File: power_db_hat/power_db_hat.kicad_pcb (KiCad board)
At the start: 4 copper layers, 65 x 56 mm, 151 parts, among them J1 Conn_01x02_Pin, J10 Screw_Terminal_01x02, J11 Conn_01x03_Pin, J12 Conn_01x03_Pin, J15 Screw_Terminal_01x02, J16 Screw_Terminal_01x02, J2 BAT2, J3 Screw_Terminal_01x02, J4 Screw_Terminal_01x02, J5 24V_out, J6 Conn_01x02_Pin, J7 Screw_Terminal_01x02, J8 BAT1, Q1 FDS6681Z, Q2 FDS6681Z, Q6 SIS468DN, Q7 SIS468DN, U1 INA3221, U2 LDD-700LS, U3 MAX17506ATP+T, U4 TL431DBZ, U5 MAX17506ATP+T, U6 LDD-700LS, U7 B2B pins, U8 DRV8212P, U9 DRV8212P

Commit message: lol
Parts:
- removed D52: D_Schottky, Diode_SMD:D_SMA-SMB_Universal_Handsoldering
- removed D6: D_Schottky, Diode_SMD:D_SMB_Handsoldering
- added J3: Screw_Terminal_01x02, TerminalBlock:TerminalBlock_Xinya_XY308-2.54-2P_1x02_P2.54mm_Horizontal, F.Cu at (2.04, 3.62)
- added J7: Screw_Terminal_01x02, TerminalBlock:TerminalBlock_Xinya_XY308-2.54-2P_1x02_P2.54mm_Horizontal, F.Cu at (9.69, 3.62)
- added Q3: BC847, Package_TO_SOT_SMD:SOT-23, F.Cu at (105.9, 146.1)
- added Q4: FDS6681Z, FDS6681Z:FDS6681Z_SOP-8, F.Cu at (107.8, 139.9)
- added R3: 10k, Resistor_SMD:R_0603_1608Metric_Pad0.98x0.95mm_HandSolder, F.Cu at (124.7, 142.8)
- added R4: 100k, Resistor_SMD:R_0603_1608Metric_Pad0.98x0.95mm_HandSolder, F.Cu at (124.7, 145.3)
- added R5: 100k, Resistor_SMD:R_0603_1608Metric_Pad0.98x0.95mm_HandSolder, F.Cu at (124.7, 147.8)
- C10, C19, C20, C25, C26, C5, JP10, JP11, JP12, JP2, JP3, JP9, R1, U1: moved to B.Cu
- C17, C27, C28: moved to F.Cu
- L1: footprint IND_B82477G4472M000:IND_B82477G4472M000 -> B82477G4472M000:IND_B82477G4472M000
- L2: footprint IND_B82477G4472M000:IND_B82477G4472M000 -> Inductor_SMD:L_TDK_VLS6045EX_VLS6045AF; moved to B.Cu
- Q6, Q7: footprint Package_SO:Vishay_PowerPAK_1212-8_Single -> SiS468DN:Vishay_PowerPAK_1212-8_Single
- U8, U9: footprint Package_SON:WSON-8-1EP_2x2mm_P0.5mm_EP0.9x1.6mm_ThermalVias -> Package_SON:WSON-8-1EP_2x2mm_P0.5mm_EP0.9x1.6mm; moved to B.Cu
- moved C16 114.4 mm to (123.1, 73.0)
- moved C29 108.7 mm to (126.9, 65.0), turned to 0 degrees
- moved R20 108.2 mm to (119.5, 73.0), turned to 0 degrees
- moved R19 100.9 mm to (126.0, 62.0), turned to 90 degrees
- moved C39 97.9 mm to (133.4, 59.5)
- moved C41 96.8 mm to (133.4, 62.0)
- moved C43 94.0 mm to (133.4, 64.5)
- moved L2 82.4 mm to (139.5, 64.0), turned to 90 degrees
- moved JP10 80.3 mm to (129.5, 73.5), turned to 180 degrees
- moved C17 77.3 mm to (119.5, 58.5), turned to 90 degrees
- moved C27 76.4 mm to (122.0, 58.5), turned to 90 degrees
- moved C28 75.6 mm to (124.5, 58.5), turned to 90 degrees
- moved R44 75.3 mm to (147.4, 70.0)
- moved R66 75.1 mm to (147.4, 72.5)
- moved Q6 71.6 mm to (147.0, 66.0)
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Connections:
- U8 pad 2: Net-(J3-Pin_1) -> Net-(J3-Pin_2)
- U8 pad 3: Net-(J3-Pin_2) -> Net-(J3-Pin_1)
- U9 pad 2: Net-(J7-Pin_1) -> Net-(J7-Pin_2)
- U9 pad 3: Net-(J7-Pin_2) -> Net-(J7-Pin_1)
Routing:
- net Net-(U3-EN/UVLO): track 0.00 -> 7.21 mm
- net Net-(Q7-D): track 0.00 -> 7.05 mm, vias 0 -> 4
- net +24V: track 3.16 -> 10.2 mm
- net Net-(U3-EXTVCC): track 0.00 -> 5.52 mm
- net Net-(U3-SS): track 0.00 -> 2.97 mm
- net Net-(U3-*RESET): track 0.00 -> 2.67 mm
- net Net-(JP10-A): track 0.00 -> 2.61 mm
- net Net-(U3-BST): track 0.00 -> 2.48 mm
- net Net-(Q7-G): track 0.00 -> 2.38 mm
- net Net-(U3-DL): track 0.00 -> 2.07 mm
- added copper zone on F.Cu, net +24V
- added copper zone on B.Cu, net Net-(Q7-D)
- added copper zone on F.Cu, net Net-(Q7-D)

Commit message: lol
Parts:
- removed JP4, JP6: SolderJumper_2_Open, Jumper:SolderJumper-2_P1.3mm_Open_TrianglePad1.0x1.5mm
- moved R29 105.8 mm to (97.1, 39.5)
- moved R5 95.6 mm to (117.0, 52.5), turned to 180 degrees
- moved Q3 95.4 mm to (122.0, 52.0), turned to 180 degrees
- moved R4 91.3 mm to (127.5, 54.0), turned to 90 degrees
- moved R3 88.8 mm to (125.5, 54.0), turned to -90 degrees
- moved Q4 84.1 mm to (118.5, 56.5), turned to 180 degrees
- moved R34 71.5 mm to (120.5, 54.5), turned to 90 degrees
- moved JP9 53.2 mm to (202.4, 88.7)
- moved L2 53.2 mm to (190.1, 80.2)
- moved Q6 53.2 mm to (197.6, 82.2)
- moved R44 53.2 mm to (198.0, 86.2)
- moved R66 53.2 mm to (198.0, 88.7)
- moved U1 53.2 mm to (194.8, 94.5)
- moved U5 53.2 mm to (190.1, 87.7)
- moved U8 53.2 mm to (204.6, 95.5)
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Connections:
- R33 pad 1: /power/VOUT_12V -> +12V
- R34 pad 1: /power/5V_OUT -> +5V
- U1 pad 1: /power/5V_OUT -> +5V
- U1 pad 14: /power/VOUT_12V -> +12V
- U7 pad 10b: GND -> +5V
- U7 pad 11b: +3V3 -> /I2C_SDA
- U7 pad 12b: /I2C_SCL -> +5V
- U7 pad 1b: +5V -> GND
- U7 pad 2b: +5V -> GND
- U7 pad 6b: GND -> +5V
- U7 pad 6c: GND -> unconnected-(U7-Pad6c)
- U7 pad 7b: +5V -> /I2C_SCL
- U7 pad 8b: /I2C_SDA -> +5V
- U7 pad 8c: GND -> +3V3
- U7 pad 9b: +3V3 -> GND
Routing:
- net +24V: track 10.2 -> 1.29 mm, vias 22 -> 24
- net Net-(Q7-D): track 7.05 -> 3.33 mm, vias 4 -> 0
- net Net-(JP10-A): track 2.61 -> 0.00 mm
- net Net-(Q7-G): track 2.38 -> 0.00 mm
- net Net-(U3-EN/UVLO): track 7.21 -> 5.21 mm
- removed copper zone on B.Cu, net Net-(Q7-D)
- removed copper zone on F.Cu, net Net-(Q7-D)

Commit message: LMAO
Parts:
- removed the J3 at (2.04, 3.62)
- removed the J7 at (9.69, 3.62)
- C10, C19, C20, C25, C26, C5, JP11, JP12, JP2, JP3, JP9, L2, R1, R34, U1, U8, U9: moved to F.Cu
- moved U1 104.9 mm to (90.0, 90.5), turned to 0 degrees
- moved C39 89.9 mm to (231.1, 63.7)
- moved C41 89.4 mm to (228.6, 79.0)
- moved C43 85.6 mm to (226.8, 53.7)
- moved C10 69.0 mm to (238.2, 121.8), turned to 0 degrees
- moved C19 69.0 mm to (238.2, 124.3), turned to 0 degrees
- moved C5 69.0 mm to (238.2, 119.3), turned to 0 degrees
- moved R1 69.0 mm to (238.2, 139.3), turned to 0 degrees
- moved R2 69.0 mm to (238.2, 141.8)
- moved JP9 47.1 mm to (181.7, 131.0)
- moved JP11 44.1 mm to (181.7, 119.9), turned to 0 degrees
- moved JP12 44.1 mm to (181.7, 123.4), turned to 0 degrees
- moved Q6 35.8 mm to (217.3, 52.4)
- moved R44 33.1 mm to (222.4, 63.7)
- moved L2 32.7 mm to (210.5, 105.8), turned to 0 degrees
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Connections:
- C16 pad 2: Net-(Q7-D) -> /power/5V_SNS+
- C37 pad 2: Net-(Q6-D) -> /power/12V_SNS+
- C39 pad 1: /power/12V_SNS -> +12V
- C41 pad 1: /power/12V_SNS -> +12V
- C43 pad 1: /power/12V_SNS -> +12V
- L1 pad 1: Net-(Q7-D) -> /power/5V_SNS-
- L2 pad 1: Net-(Q6-D) -> /power/12V_SNS-
- L2 pad 2: /power/12V_SNS -> +12V
- Q4 pad 3: /power/5V_SNS -> +5V
- Q6 pad 1: Net-(Q6-D) -> /power/12V_SNS+
- Q7 pad 1: Net-(Q7-D) -> /power/5V_SNS+
- R33 pad 1: +12V -> /power/12V_SNS-
- R33 pad 2: /power/12V_SNS -> /power/12V_SNS+
- R34 pad 1: +5V -> /power/5V_SNS-
- R34 pad 2: /power/5V_SNS -> /power/5V_SNS+
- R35 pad 1: /power/12V_SNS -> +12V
- R38 pad 1: /power/12V_SNS -> +12V
- R42 pad 2: /power/12V_SNS -> +12V
- R5 pad 2: /power/5V_SNS -> +5V
- U1 pad 1: +5V -> /power/5V_SNS-
- U1 pad 14: +12V -> /power/12V_SNS+
- U1 pad 15: /power/12V_SNS -> /power/12V_SNS-
- U1 pad 2: /power/5V_SNS -> /power/5V_SNS+
- U3 pad 17: Net-(Q7-D) -> /power/5V_SNS+
- U3 pad 18: Net-(Q7-D) -> /power/5V_SNS+
- U3 pad 19: Net-(Q7-D) -> /power/5V_SNS+
- U5 pad 17: Net-(Q6-D) -> /power/12V_SNS+
- U5 pad 18: Net-(Q6-D) -> /power/12V_SNS+
- U5 pad 19: Net-(Q6-D) -> /power/12V_SNS+
- U7 pad 10b: +5V -> GND
- U7 pad 12b: +5V -> /I2C_SCL
- U7 pad 1b: GND -> +5V
- U7 pad 2b: GND -> +5V
- U7 pad 7b: /I2C_SCL -> +5V
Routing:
- net +24V: track 1.29 -> 7.05 mm, vias 24 -> 0
- net Net-(Q7-D): track 3.33 -> 0.00 mm
- net /power/5V_SNS+: track 0.00 -> 3.33 mm
- net Net-(JP10-A): track 0.00 -> 2.61 mm
- net Net-(U3-EN/UVLO): track 5.21 -> 7.21 mm
- net Net-(U3-VCC): track 2.53 -> 2.02 mm
- net +5V: vias 0 -> 5
- added copper zone on B.Cu, net +5V
- added copper zone on F.Cu, net +5V
- removed copper zone on F.Cu, net +24V

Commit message: lol
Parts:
- removed JP10, JP11, JP12, JP9: SolderJumper_2_Open, Jumper:SolderJumper-2_P1.3mm_Open_TrianglePad1.0x1.5mm
- C10, C19, C20, C25, C26, C44, C5, JP2, JP3, R1, R2, U1, U8, U9: moved to B.Cu
- moved C44 126.6 mm to (133.4, 65.8), turned to 180 degrees
- moved C9 125.1 mm to (126.0, 68.8), turned to -90 degrees
- moved C11 122.4 mm to (128.5, 68.8), turned to -90 degrees
- moved C13 119.8 mm to (131.0, 68.8), turned to -90 degrees
- moved R1 106.3 mm to (152.2, 76.8), turned to 90 degrees
- moved R23 105.1 mm to (121.8, 61.2), turned to 90 degrees
- moved R22 102.8 mm to (124.0, 61.2), turned to -90 degrees
- moved R2 102.1 mm to (152.6, 86.2), turned to 180 degrees
- moved C10 96.5 mm to (154.0, 74.6), turned to 90 degrees
- moved C20 95.5 mm to (152.6, 84.4), turned to 180 degrees
- moved C19 94.8 mm to (156.8, 75.6), turned to 180 degrees
- moved C26 94.5 mm to (156.6, 84.1), turned to 180 degrees
- moved C25 94.1 mm to (156.6, 82.4), turned to 180 degrees
- moved C5 93.2 mm to (156.8, 73.8), turned to 180 degrees
- moved U9 53.5 mm to (156.6, 86.2), turned to 180 degrees
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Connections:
- C16 pad 2: /power/5V_SNS+ -> Net-(Q7-D)
- C17 pad 1: /power/bucks/BUCK_OUT_5V -> /power/5V_SNS-
- C27 pad 1: /power/bucks/BUCK_OUT_5V -> /power/5V_SNS-
- C28 pad 1: /power/bucks/BUCK_OUT_5V -> /power/5V_SNS-
- L1 pad 1: /power/5V_SNS- -> Net-(Q7-D)
- L1 pad 2: /power/bucks/BUCK_OUT_5V -> /power/5V_SNS+
- Q4 pad 1: /power/bucks/BUCK_OUT_5V -> /power/5V_SNS-
- Q7 pad 1: /power/5V_SNS+ -> Net-(Q7-D)
- R19 pad 2: /power/bucks/BUCK_OUT -> /power/5V_SNS-
- R22 pad 1: /power/bucks/BUCK_OUT_5V -> /power/5V_SNS-
- R3 pad 2: /power/bucks/BUCK_OUT_5V -> /power/5V_SNS-
- R30 pad 1: /power/bucks/BUCK_OUT_5V -> /power/5V_SNS-
- R65 pad 1: Net-(JP10-A) -> +24V
- R66 pad 1: Net-(JP9-A) -> +24V
- U3 pad 17: /power/5V_SNS+ -> Net-(Q7-D)
- U3 pad 18: /power/5V_SNS+ -> Net-(Q7-D)
- U3 pad 19: /power/5V_SNS+ -> Net-(Q7-D)
- U7 pad 10c: GND -> /LED_PWM_1
- U7 pad 11c: /LED_PWM_2 -> GND
- U7 pad 12c: GND -> /LED_PWM_2
- U7 pad 1c: /MOTOR_1_A -> /SERVO_2
- U7 pad 2c: /SERVO_1 -> /MOTOR_1_B
- U7 pad 3c: /MOTOR_1_B -> /SERVO_1
- U7 pad 4c: /SERVO_2 -> /MOTOR_1_A
- U7 pad 5c: /MOTOR_2_A -> +3V3
- U7 pad 6c: unconnected-(U7-Pad6c) -> /MOTOR_2_B
- U7 pad 7c: /MOTOR_2_B -> +3V3
- U7 pad 8c: +3V3 -> /MOTOR_2_A
- U7 pad 9c: /LED_PWM_1 -> GND
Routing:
- net /MOTOR_2_A: track 0.00 -> 48.6 mm
- net +3V3: track 0.00 -> 47.9 mm, vias 0 -> 3
- net /MOTOR_2_B: track 0.00 -> 47.5 mm
- net /MOTOR_1_A: track 0.00 -> 42.2 mm
- net /MOTOR_1_B: track 0.00 -> 40.6 mm
- net /LED_PWM_2: track 0.00 -> 28.7 mm, vias 0 -> 1
- net /SERVO_1: track 0.00 -> 27.8 mm
- net /SERVO_2: track 0.00 -> 12.7 mm
- net /power/5V_SNS-: track 0.00 -> 7.71 mm
- net /expansion/V_ACT: track 0.00 -> 6.88 mm
- net GND: track 0.48 -> 5.37 mm
- net Net-(U3-FB): track 0.00 -> 4.80 mm
- net Net-(J3-Pin_1): track 0.00 -> 4.58 mm
- net Net-(J3-Pin_2): track 0.00 -> 3.98 mm
- net Net-(J7-Pin_2): track 0.00 -> 3.42 mm
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- added copper zone on F.Cu, net /power/5V_SNS+
- added copper zone on F.Cu, net /power/5V_SNS-
- added copper zone on B.Cu, net Net-(Q7-D)

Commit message: damo was here
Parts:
- removed C2, C4, C49: 100nF, Capacitor_SMD:C_0603_1608Metric_Pad1.08x0.95mm_HandSolder
- removed C50: 22uF, Capacitor_SMD:C_0603_1608Metric_Pad1.08x0.95mm_HandSolder
- removed D45, D46: TVS_3V3, Diode_SMD:D_0603_1608Metric_Pad1.05x0.95mm_HandSolder
- removed JP1: SolderJumper_2_Open, Jumper:SolderJumper-2_P1.3mm_Open_TrianglePad1.0x1.5mm
- removed R30, R38: 10k, Resistor_SMD:R_0603_1608Metric_Pad0.98x0.95mm_HandSolder
- C1, C23, C24, D41, L2: moved to B.Cu
- C44: moved to F.Cu
- moved R13 139.2 mm to (102.4, 57.9), turned to 180 degrees
- moved R12 139.1 mm to (102.4, 55.9), turned to 180 degrees
- moved R11 139.0 mm to (102.4, 53.9), turned to 180 degrees
- moved R10 137.3 mm to (102.4, 51.9), turned to 180 degrees
- moved C47 126.0 mm to (113.2, 45.1)
- moved C48 126.0 mm to (113.2, 47.6), turned to 180 degrees
- moved C23 125.5 mm to (134.3, 48.4), turned to -90 degrees
- moved C1 122.3 mm to (108.5, 74.7)
- moved C24 117.9 mm to (143.5, 48.8), turned to -90 degrees
- moved C30 116.8 mm to (132.3, 85.1)
- moved C43 113.2 mm to (116.8, 80.6), turned to 90 degrees
- moved C39 110.6 mm to (121.8, 80.6), turned to 90 degrees
- moved C41 109.3 mm to (119.3, 80.6), turned to 90 degrees
- moved C31 101.2 mm to (134.5, 71.0), turned to 90 degrees
- moved C32 100.6 mm to (132.5, 71.0), turned to 90 degrees
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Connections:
- C37 pad 2: /power/12V_SNS+ -> Net-(Q6-D)
- JP2 pad 1: /expansion/V_ACT -> +5V
- JP2 pad 2: +5V -> /expansion/V_ACT
- L2 pad 1: /power/12V_SNS- -> Net-(Q6-D)
- L2 pad 2: +12V -> /power/12V_SNS+
- Q6 pad 1: /power/12V_SNS+ -> Net-(Q6-D)
- R33 pad 1: /power/12V_SNS- -> +12V
- U1 pad 15: /power/12V_SNS- -> +12V
- U1 pad 4: Net-(JP1-B) -> +3V3
- U3 pad 6: Net-(U3-*RESET) -> unconnected-(U3-*RESET-Pad6)
- U5 pad 17: /power/12V_SNS+ -> Net-(Q6-D)
- U5 pad 18: /power/12V_SNS+ -> Net-(Q6-D)
- U5 pad 19: /power/12V_SNS+ -> Net-(Q6-D)
- U5 pad 6: Net-(U5-*RESET) -> unconnected-(U5-*RESET-Pad6)
- U7 pad 11b: /I2C_SDA -> /I2C_SCL
- U7 pad 11c: GND -> /IND
- U7 pad 12b: /I2C_SCL -> /I2C_SDA
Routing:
- net +12V: track 0.00 -> 145.9 mm, vias 0 -> 6
- net +3V3: track 47.9 -> 135.8 mm, vias 3 -> 7
- net /power/24V_SNS: track 2.48 -> 52.6 mm, vias 15 -> 12
- net +5V: track 0.00 -> 43.0 mm, vias 5 -> 35
- net /IND: track 0.00 -> 40.1 mm, vias 0 -> 1
- net /LED_PWM_1: track 3.30 -> 36.6 mm, vias 0 -> 1
- net /I2C_SDA: track 0.00 -> 30.3 mm
- net /power/12V_SNS+: track 0.00 -> 29.4 mm
- net /I2C_SCL: track 0.00 -> 28.3 mm
- net /power/5V_SNS-: track 7.71 -> 29.3 mm, vias 0 -> 1
- net +24V: track 4.31 -> 25.9 mm, vias 11 -> 21
- net /expansion/V_ACT: track 6.88 -> 23.2 mm, vias 0 -> 2
- net /power/5V_SNS+: track 0.00 -> 16.0 mm, vias 0 -> 1
- net Net-(Q6-G): track 0.00 -> 14.9 mm
- net Net-(JP5-A): track 0.00 -> 8.74 mm
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- added copper zone on F.Cu, net /VBAT1+
- added copper zone on In1.Cu, net /VBAT1+
- added copper zone on B.Cu, net GND
- added copper zone on F.Cu, net GND
- added copper zone on B.Cu, net Net-(Q6-D)
- added copper zone on F.Cu, net Net-(Q7-D)
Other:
- board text added: "{ "ViaStitching": "0.4", "stitch_zone_0": { "HSpacing": "3", "VSpacing": "3", "HOffset": "0", "VOffset": "0", "EdgeMargin": "0", "PadMargin": "0", "Clearance": "0", "ViaSize": "0.6", "ViaDrill": "0.3", "Randomize": false, "ClearOwn": true, "IncludeOtherLayers": true, "BlockFootprintZones": true, "AllowUnderPadSameNet": false, "TargetViaCountMode": false, "TargetViaCount": "100", "TargetPattern": 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"
- board text removed: "Extend PCB edge 0.5mm if using SMT header"

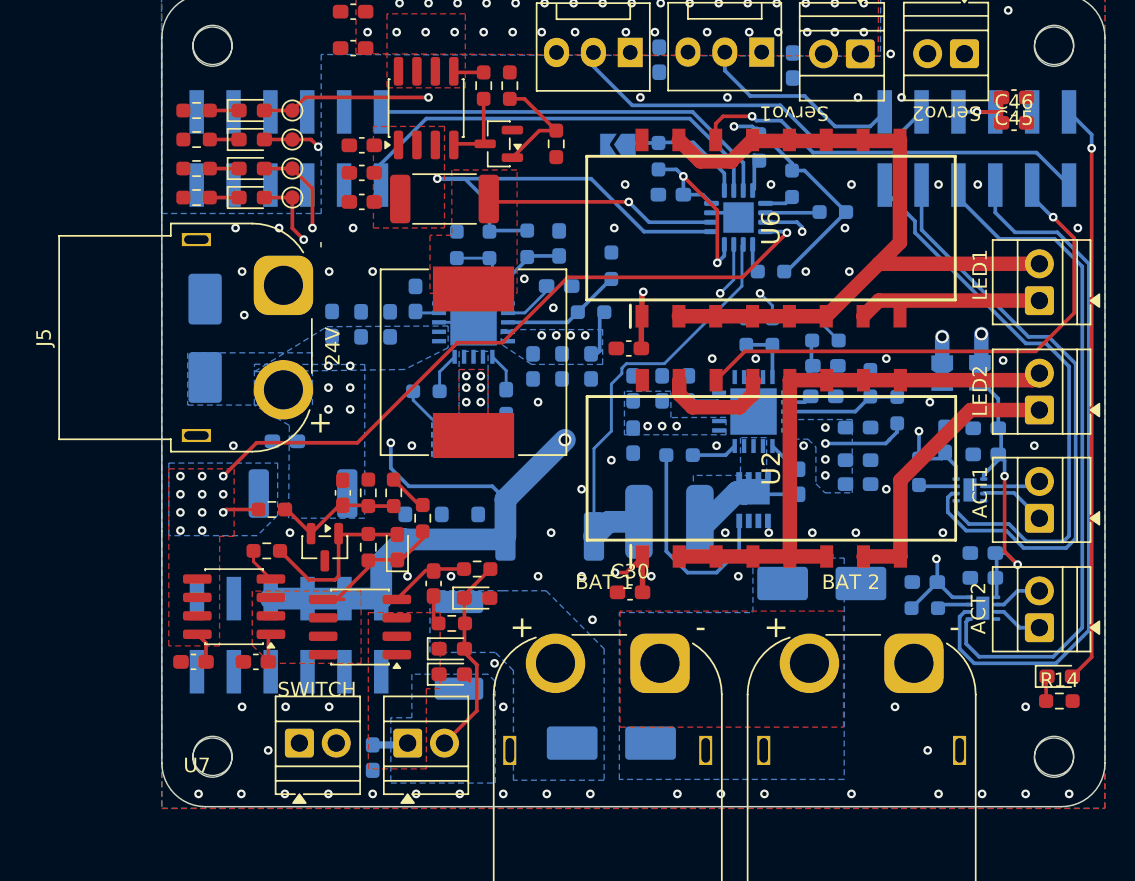
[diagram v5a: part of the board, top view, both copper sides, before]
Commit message: updated 3d models for power
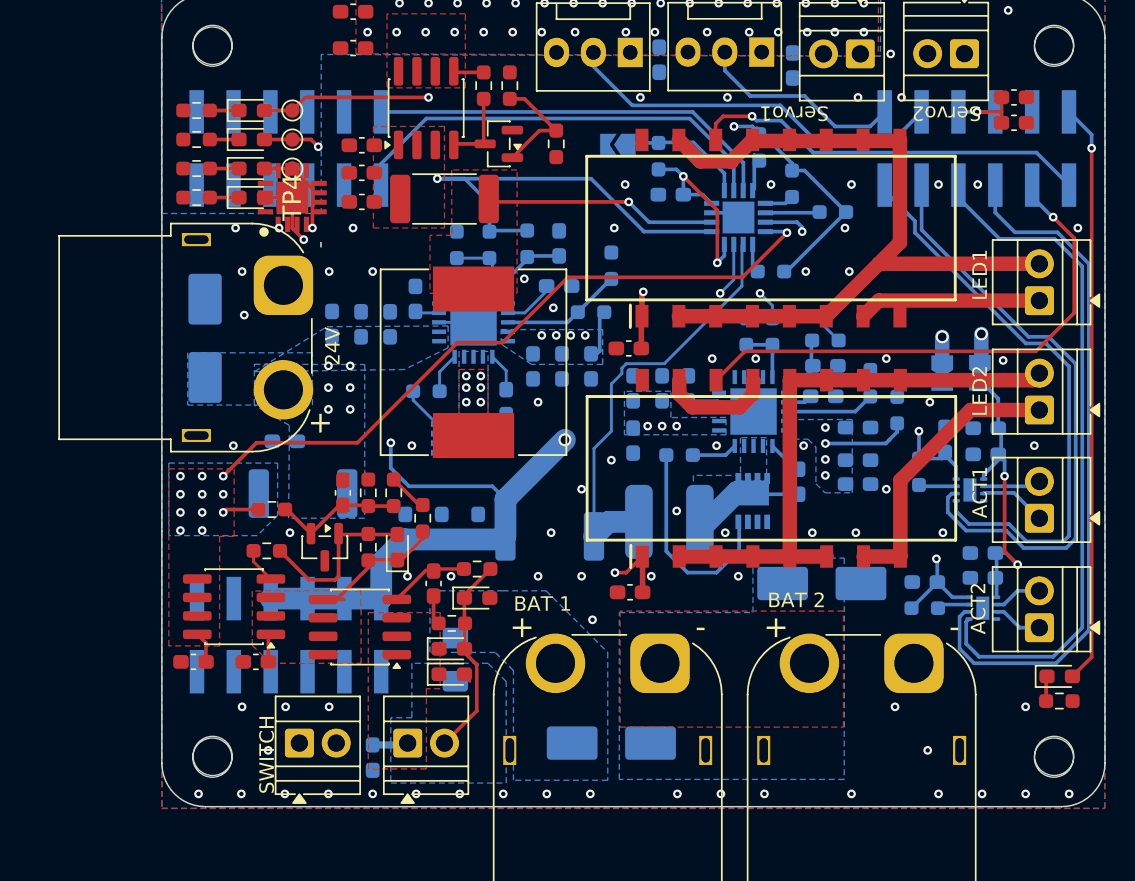
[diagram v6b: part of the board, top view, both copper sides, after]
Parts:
- removed Q6: SIS468DN, SiS468DN:Vishay_PowerPAK_1212-8_Single
- added Q5: SIS468DN-T1-GE3, SiS468DN-T1-GE3:VISHAY_SIS468DN-T1-GE3, B.Cu at (120.5, 74.5)
- F1: value FUSE_10A -> FUSE_15A; footprint Fuse:Fuse_2512_6332Metric_Pad1.52x3.35mm_HandSolder -> Fuse:Fuse_1206_3216Metric_Pad1.42x1.75mm_HandSolder
- J1, J10, J15, J16, J3, J4, J6, J7: footprint TerminalBlock:TerminalBlock_Xinya_XY308-2.54-2P_1x02_P2.54mm_Horizontal -> Terminal_Block_Custom:1x02_P2.54mm_Horizontal
- Q7: value SIS468DN -> SIS468DN-T1-GE3; footprint SiS468DN:Vishay_PowerPAK_1212-8_Single -> SiS468DN-T1-GE3:VISHAY_SIS468DN-T1-GE3
- TP4: footprint TestPoint:TestPoint_Pad_D1.0mm -> INA3221:QFN65P400X400X100-17N-D
- U1: footprint Package_DFN_QFN:Texas_RGV0016A_VQFN-16-1EP_4x4mm_P0.65mm_EP2.1x2.1mm -> INA3221:QFN65P400X400X100-17N-D
- moved Q7 20.7 mm to (140.7, 78.8), turned to 90 degrees
- moved F1 1.02 mm to (120.2, 89.8)
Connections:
- C16 pad 2: Net-(Q7-D) -> Net-(C16-Pad2)
- C37 pad 2: Net-(Q6-D) -> Net-(C37-Pad2)
- L1 pad 1: Net-(Q7-D) -> Net-(C16-Pad2)
- L2 pad 1: Net-(Q6-D) -> Net-(C37-Pad2)
- Q7 pad 1: Net-(Q7-D) -> GND
- Q7 pad 2: Net-(Q7-G) -> GND
- R20 pad 1: Net-(Q7-G) -> Net-(Q5-Pad4)
- R43 pad 1: Net-(Q6-G) -> Net-(Q7-Pad4)
- U3 pad 17: Net-(Q7-D) -> Net-(C16-Pad2)
- U3 pad 18: Net-(Q7-D) -> Net-(C16-Pad2)
- U3 pad 19: Net-(Q7-D) -> Net-(C16-Pad2)
- U5 pad 17: Net-(Q6-D) -> Net-(C37-Pad2)
- U5 pad 18: Net-(Q6-D) -> Net-(C37-Pad2)
- U5 pad 19: Net-(Q6-D) -> Net-(C37-Pad2)
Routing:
- net Net-(Q7-Pad4): track 0.00 -> 14.9 mm
- net Net-(Q6-G): track 14.9 -> 0.00 mm
- net Net-(Q6-D): track 7.22 -> 0.00 mm
- net Net-(C37-Pad2): track 0.00 -> 7.22 mm
- net Net-(Q7-D): track 3.40 -> 0.00 mm, vias 6 -> 0
- net Net-(C16-Pad2): track 0.00 -> 3.40 mm, vias 0 -> 6
- net Net-(Q7-G): track 3.06 -> 0.00 mm
- net Net-(Q5-Pad4): track 0.00 -> 3.06 mm
- net GND: vias 80 -> 77
- net +24V: vias 21 -> 22
- added copper zone on B.Cu, net Net-(C16-Pad2)
- added copper zone on F.Cu, net Net-(C16-Pad2)
- added copper zone on B.Cu, net Net-(C37-Pad2)
- removed copper zone on B.Cu, net Net-(Q6-D)
- removed copper zone on B.Cu, net Net-(Q7-D)
- removed copper zone on F.Cu, net Net-(Q7-D)

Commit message: working on BOM
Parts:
- removed TP4: TestPoint, INA3221:QFN65P400X400X100-17N-D
- moved C45 0.56 mm to (159.2, 51.2)
- moved C46 0.56 mm to (159.2, 53.0)
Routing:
- net Net-(J1-Pin_2): track 47.6 -> 50.1 mm
- net +24V: track 25.9 -> 24.5 mm, vias 22 -> 21
- net Net-(Q1-G): track 4.98 -> 5.49 mm
- net GND: track 7.37 -> 7.02 mm, vias 77 -> 71

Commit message: complete BOM
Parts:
- removed D15, D43: TVS_26V, Diode_SMD:D_0603_1608Metric_Pad1.05x0.95mm_HandSolder
- removed D8: TVS_13V, Diode_SMD:D_SMB_Handsoldering
- added TP4: TestPoint, TestPoint:TestPoint_Pad_D1.0mm, F.Cu at (109.0, 57.8)
- D10, D9: footprint Diode_SMD:D_SMB_Handsoldering -> Diode_SMD:D_SMA_Handsoldering
- D11, D7: footprint Diode_SMD:D_0603_1608Metric_Pad1.05x0.95mm_HandSolder -> Diode_SMD:D_SOD-323_HandSoldering
- D41: footprint Diode_SMD:D_0603_1608Metric_Pad1.05x0.95mm_HandSolder -> Diode_SMD:D_SMA_Handsoldering; moved to F.Cu
- moved D41 18.1 mm to (125.4, 82.1), turned to 90 degrees
- moved D9 0.50 mm to (146.0, 84.5)
- moved D7 0.21 mm to (116.2, 82.2)
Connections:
- D41 pad 1: /VBAT_24V -> /VBAT2+
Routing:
- net /VBAT2+: track 0.00 -> 6.16 mm
- net /VBAT_24V: track 4.49 -> 2.20 mm
- net /power/5V_SNS-: track 29.3 -> 31.3 mm, vias 1 -> 2
- net GND: vias 71 -> 69
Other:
- board text added: "ALTAIR Power HAT Ben D'Agnillo March 2026 - v1.0"
